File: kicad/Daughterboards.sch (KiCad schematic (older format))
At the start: 6 parts

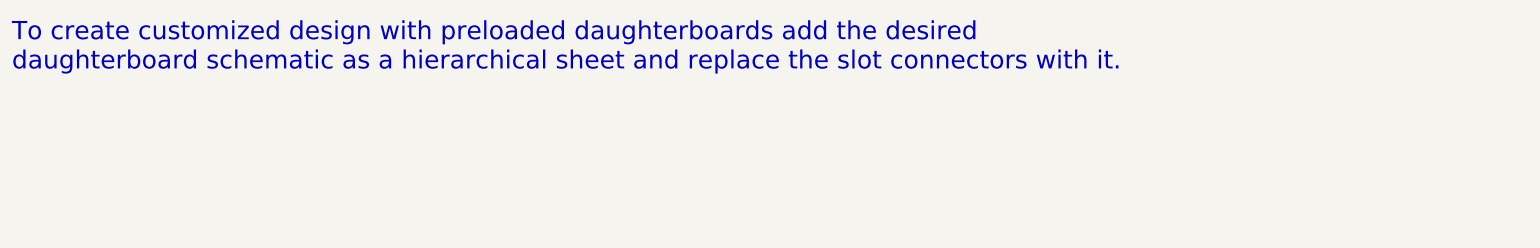
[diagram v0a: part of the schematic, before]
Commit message: Completed data and power isolation sheets
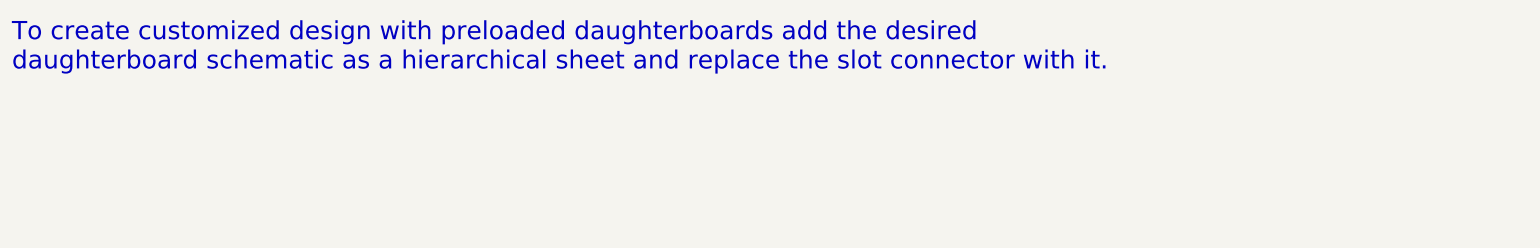
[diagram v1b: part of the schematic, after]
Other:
- note added: "To create customized design with preloaded daughterboards add the desired \ndaughterboard schematic as a hierarchical sheet and replace the slot connector with it."
- note removed: "To create customized design with preloaded daughterboards add the desired \ndaughterboard schematic as a hierarchical sheet and replace the slot connectors with it."
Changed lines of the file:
@@
 LIBS:+5v_iso
 LIBS:gnd_iso
+LIBS:roe-0505s
+LIBS:si8660
 LIBS:Main-cache
 EELAYER 27 0
@@
 	7400 5150 7550 5150
 Text Notes 1000 1150 0    120  ~ 0
-To create customized design with preloaded daughterboards add the desired \ndaughterboard schematic as a hierarchical sheet and replace the slot connectors with it.
+To create customized design with preloaded daughterboards add the desired \ndaughterboard schematic as a hierarchical sheet and replace the slot connector with it.
 Wire Wire Line
 	5700 4950 5850 4950

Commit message: ID detection changed from RC to EEPROM based, D.board pinout changed, PIC18F85J94 added
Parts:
- removed P?: SLOT0, symbol CONN_10
- removed P?: SLOT1, symbol CONN_10
- removed P?: SLOT2, symbol CONN_10
- removed P?: SLOT3, symbol CONN_10
- removed P?: SLOT4, symbol CONN_10
- removed P?: SLOT5, symbol CONN_10
- added P?: SLOT_A, symbol CONN_12
- added P?: SLOT_B, symbol CONN_12
- added P?: SLOT_C, symbol CONN_12
- added P?: SLOT_D, symbol CONN_12
- added P?: SLOT_E, symbol CONN_12
- added P?: SLOT_F, symbol CONN_12
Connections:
- net labels added: ID_3.3V, ID_GND, ID_SCL, ID_SDA, RTS3, VCC
- net labels removed: ID0, ID1, ID2, ID3, ID4, ID5, ID_COM, RT3, VCC_5V
- wire segments 60 -> 72
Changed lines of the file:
@@
 LIBS:si8660
 LIBS:pic16f1704
+LIBS:PIC18F85J94
+LIBS:24AA014
 LIBS:Main-cache
 EELAYER 27 0
@@
 $Descr A4 11693 8268
 encoding utf-8
-Sheet 7 8
+Sheet 7 7
 Title ""
-Date "22 jun 2014"
+Date "23 jun 2014"
 Rev ""
 Comp ""
@@
 Comment4 ""
 $EndDescr
-$Comp
-L CONN_10 P?
-U 1 1 53A642AA
-P 4500 3100
-F 0 "P?" V 4450 3100 60  0000 C CNN
-F 1 "SLOT0" V 4550 3100 60  0000 C CNN
-F 2 "" H 4500 3100 60  0000 C CNN
-F 3 "" H 4500 3100 60  0000 C CNN
-	1    4500 3100
-	1    0    0    -1
-$EndComp
 Text HLabel 4000 2750 0    60   Output ~ 0
 RX0
@@
 Wire Wire Line
 	4150 3150 4000 3150
+Text HLabel 4000 3250 0    60   Input ~ 0
+VCC
+Wire Wire Line
+	4000 3250 4150 3250
+Text HLabel 4000 3350 0    60   Input ~ 0
+GND
+Text HLabel 4000 3550 0    60   BiDi ~ 0
+ID_SDA
+Wire Wire Line
+	4000 3350 4150 3350
+Wire Wire Line
+	4000 3450 4150 3450
+Wire Wire Line
+	4000 3550 4150 3550
+Text Notes 1000 1150 0    120  ~ 0
+To create customized design with preloaded daughterboards add the desired \ndaughterboard schematic as a hierarchical sheet and replace the slot connector with it.
+Text HLabel 4000 3650 0    60   BiDi ~ 0
+ID_SCL
+Text Notes 3750 6650 0    60   ~ 0
+All pins at 5V TTL level
+$Comp
+L CONN_12 P?
+U 1 1 53B6335B
+P 4500 3200
+F 0 "P?" V 4450 3200 60  0000 C CNN
+F 1 "SLOT_A" V 4550 3200 60  0000 C CNN
+F 2 "" H 4500 3200 60  0000 C CNN
+F 3 "" H 4500 3200 60  0000 C CNN
+	1    4500 3200
+	1    0    0    -1
+$EndComp
+Wire Wire Line
+	4000 3650 4150 3650
 Text HLabel 4000 3450 0    60   Input ~ 0
-VCC_5V
-Wire Wire Line
-	4000 3250 4150 3250
-Text HLabel 4000 3550 0    60   Input ~ 0
-GND
-Text HLabel 4000 3250 0    60   BiDi ~ 0
-ID0
-Wire Wire Line
-	4000 3350 4150 3350
-Wire Wire Line
-	4000 3450 4150 3450
-Wire Wire Line
-	4000 3550 4150 3550
-$Comp
-L CONN_10 P?
-U 1 1 53A64390
-P 6200 3100
-F 0 "P?" V 6150 3100 60  0000 C CNN
-F 1 "SLOT1" V 6250 3100 60  0000 C CNN
-F 2 "" H 6200 3100 60  0000 C CNN
-F 3 "" H 6200 3100 60  0000 C CNN
-	1    6200 3100
-	1    0    0    -1
-$EndComp
+ID_3.3V
+Text HLabel 4000 3750 0    60   Input ~ 0
+ID_GND
+Wire Wire Line
+	4000 3750 4150 3750
 Text HLabel 5700 2750 0    60   Output ~ 0
 RX1
@@
 Wire Wire Line
 	5850 3150 5700 3150
+Text HLabel 5700 3250 0    60   Input ~ 0
+VCC
+Wire Wire Line
+	5700 3250 5850 3250
+Text HLabel 5700 3350 0    60   Input ~ 0
+GND
+Text HLabel 5700 3550 0    60   BiDi ~ 0
+ID_SDA
+Wire Wire Line
+	5700 3350 5850 3350
+Wire Wire Line
+	5700 3450 5850 3450
+Wire Wire Line
+	5700 3550 5850 3550
+Text HLabel 5700 3650 0    60   BiDi ~ 0
+ID_SCL
+$Comp
+L CONN_12 P?
+U 1 1 53B634CC
+P 6200 3200
+F 0 "P?" V 6150 3200 60  0000 C CNN
+F 1 "SLOT_B" V 6250 3200 60  0000 C CNN
+F 2 "" H 6200 3200 60  0000 C CNN
+F 3 "" H 6200 3200 60  0000 C CNN
+	1    6200 3200
+	1    0    0    -1
+$EndComp
+Wire Wire Line
+	5700 3650 5850 3650
 Text HLabel 5700 3450 0    60   Input ~ 0
-VCC_5V
-Wire Wire Line
-	5700 3250 5850 3250
-Text HLabel 5700 3550 0    60   Input ~ 0
-GND
-Text HLabel 5700 3250 0    60   BiDi ~ 0
-ID1
-Wire Wire Line
-	5700 3350 5850 3350
-Wire Wire Line
-	5700 3450 5850 3450
-Wire Wire Line
-	5700 3550 5850 3550
-$Comp
-L CONN_10 P?
-U 1 1 53A643DC
-P 7900 3100
-F 0 "P?" V 7850 3100 60  0000 C CNN
-F 1 "SLOT2" V 7950 3100 60  0000 C CNN
-F 2 "" H 7900 3100 60  0000 C CNN
-F 3 "" H 7900 3100 60  0000 C CNN
-	1    7900 3100
-	1    0    0    -1
-$EndComp
+ID_3.3V
+Text HLabel 5700 3750 0    60   Input ~ 0
+ID_GND
+Wire Wire Line
+	5700 3750 5850 3750
 Text HLabel 7400 2750 0    60   Output ~ 0
 RX2
@@
 Wire Wire Line
 	7550 3150 7400 3150
+Text HLabel 7400 3250 0    60   Input ~ 0
+VCC
+Wire Wire Line
+	7400 3250 7550 3250
+Text HLabel 7400 3350 0    60   Input ~ 0
+GND
+Text HLabel 7400 3550 0    60   BiDi ~ 0
+ID_SDA
+Wire Wire Line
+	7400 3350 7550 3350
+Wire Wire Line
+	7400 3450 7550 3450
+Wire Wire Line
+	7400 3550 7550 3550
+Text HLabel 7400 3650 0    60   BiDi ~ 0
+ID_SCL
+$Comp
+L CONN_12 P?
+U 1 1 53B634F5
+P 7900 3200
+F 0 "P?" V 7850 3200 60  0000 C CNN
+F 1 "SLOT_C" V 7950 3200 60  0000 C CNN
+F 2 "" H 7900 3200 60  0000 C CNN
+F 3 "" H 7900 3200 60  0000 C CNN
+	1    7900 3200
+	1    0    0    -1
+$EndComp
+Wire Wire Line
+	7400 3650 7550 3650
 Text HLabel 7400 3450 0    60   Input ~ 0
-VCC_5V
-Wire Wire Line
-	7400 3250 7550 3250
-Text HLabel 7400 3550 0    60   Input ~ 0
-GND
-Text HLabel 7400 3250 0    60   BiDi ~ 0
-ID2
-Wire Wire Line
-	7400 3350 7550 3350
-Wire Wire Line
-	7400 3450 7550 3450
-Wire Wire Line
-	7400 3550 7550 3550
-$Comp
-L CONN_10 P?
-U 1 1 53A643F6
-P 4500 4700
-F 0 "P?" V 4450 4700 60  0000 C CNN
-F 1 "SLOT3" V 4550 4700 60  0000 C CNN
-F 2 "" H 4500 4700 60  0000 C CNN
-F 3 "" H 4500 4700 60  0000 C CNN
-	1    4500 4700
-	1    0    0    -1
-$EndComp
+ID_3.3V
+Text HLabel 7400 3750 0    60   Input ~ 0
+ID_GND
+Wire Wire Line
+	7400 3750 7550 3750
 Text HLabel 4000 4350 0    60   Output ~ 0
 RX3
@@
 TX3
 Text HLabel 4000 4450 0    60   Input ~ 0
-RT3
+RTS3
 Text HLabel 4000 4550 0    60   Output ~ 0
 CTS3
@@
 Wire Wire Line
 	4150 4750 4000 4750
+Text HLabel 4000 4850 0    60   Input ~ 0
+VCC
+Wire Wire Line
+	4000 4850 4150 4850
+Text HLabel 4000 4950 0    60   Input ~ 0
+GND
+Text HLabel 4000 5150 0    60   BiDi ~ 0
+ID_SDA
+Wire Wire Line
+	4000 4950 4150 4950
+Wire Wire Line
+	4000 5050 4150 5050
+Wire Wire Line
+	4000 5150 4150 5150
+Text HLabel 4000 5250 0    60   BiDi ~ 0
+ID_SCL
+$Comp
+L CONN_12 P?
+U 1 1 53B63519
+P 4500 4800
+F 0 "P?" V 4450 4800 60  0000 C CNN
+F 1 "SLOT_D" V 4550 4800 60  0000 C CNN
+F 2 "" H 4500 4800 60  0000 C CNN
+F 3 "" H 4500 4800 60  0000 C CNN
+	1    4500 4800
+	1    0    0    -1
+$EndComp
+Wire Wire Line
+	4000 5250 4150 5250
 Text HLabel 4000 5050 0    60   Input ~ 0
-VCC_5V
-Wire Wire Line
-	4000 4850 4150 4850
-Text HLabel 4000 5150 0    60   Input ~ 0
-GND
-Text HLabel 4000 4850 0    60   BiDi ~ 0
-ID3
-Wire Wire Line
-	4000 4950 4150 4950
-Wire Wire Line
-	4000 5050 4150 5050
-Wire Wire Line
-	4000 5150 4150 5150
-$Comp
-L CONN_10 P?
-U 1 1 53A64410
-P 6200 4700
-F 0 "P?" V 6150 4700 60  0000 C CNN
-F 1 "SLOT4" V 6250 4700 60  0000 C CNN
-F 2 "" H 6200 4700 60  0000 C CNN
-F 3 "" H 6200 4700 60  0000 C CNN
-	1    6200 4700
-	1    0    0    -1
-$EndComp
+ID_3.3V
+Text HLabel 4000 5350 0    60   Input ~ 0
+ID_GND
+Wire Wire Line
+	4000 5350 4150 5350
 Text HLabel 5700 4350 0    60   Output ~ 0
 RX4
@@
 Wire Wire Line
 	5850 4750 5700 4750
+Text HLabel 5700 4850 0    60   Input ~ 0
+VCC
+Wire Wire Line
+	5700 4850 5850 4850
+Text HLabel 5700 4950 0    60   Input ~ 0
+GND
+Text HLabel 5700 5150 0    60   BiDi ~ 0
+ID_SDA
+Wire Wire Line
+	5700 4950 5850 4950
+Wire Wire Line
+	5700 5050 5850 5050
+Wire Wire Line
+	5700 5150 5850 5150
+Text HLabel 5700 5250 0    60   BiDi ~ 0
+ID_SCL
+$Comp
+L CONN_12 P?
+U 1 1 53B6353D
+P 6200 4800
+F 0 "P?" V 6150 4800 60  0000 C CNN
+F 1 "SLOT_E" V 6250 4800 60  0000 C CNN
+F 2 "" H 6200 4800 60  0000 C CNN
+F 3 "" H 6200 4800 60  0000 C CNN
+	1    6200 4800
+	1    0    0    -1
+$EndComp
+Wire Wire Line
+	5700 5250 5850 5250
 Text HLabel 5700 5050 0    60   Input ~ 0
-VCC_5V
-Wire Wire Line
-	5700 4850 5850 4850
-Text HLabel 5700 5150 0    60   Input ~ 0
-GND
-Text HLabel 5700 4850 0    60   BiDi ~ 0
-ID4
-Wire Wire Line
-	5700 5050 5850 5050
-Wire Wire Line
-	5700 5150 5850 5150
-$Comp
-L CONN_10 P?
-U 1 1 53A6442A
-P 7900 4700
-F 0 "P?" V 7850 4700 60  0000 C CNN
-F 1 "SLOT5" V 7950 4700 60  0000 C CNN
-F 2 "" H 7900 4700 60  0000 C CNN
-F 3 "" H 7900 4700 60  0000 C CNN
-	1    7900 4700
-	1    0    0    -1
-$EndComp
+ID_3.3V
+Text HLabel 5700 5350 0    60   Input ~ 0
+ID_GND
+Wire Wire Line
+	5700 5350 5850 5350
 Text HLabel 7400 4350 0    60   Output ~ 0
 RX5
@@
 Wire Wire Line
 	7550 4750 7400 4750
+Text HLabel 7400 4850 0    60   Input ~ 0
+VCC
+Wire Wire Line
+	7400 4850 7550 4850
+Text HLabel 7400 4950 0    60   Input ~ 0
+GND
+Text HLabel 7400 5150 0    60   BiDi ~ 0
+ID_SDA
+Wire Wire Line
+	7400 4950 7550 4950
+Wire Wire Line
+	7400 5050 7550 5050
+Wire Wire Line
+	7400 5150 7550 5150
+Text HLabel 7400 5250 0    60   BiDi ~ 0
+ID_SCL
+$Comp
+L CONN_12 P?
+U 1 1 53B63567
+P 7900 4800
+F 0 "P?" V 7850 4800 60  0000 C CNN
+F 1 "SLOT_F" V 7950 4800 60  0000 C CNN
+F 2 "" H 7900 4800 60  0000 C CNN
+F 3 "" H 7900 4800 60  0000 C CNN
+	1    7900 4800
+	1    0    0    -1
+$EndComp
+Wire Wire Line
+	7400 5250 7550 5250
 Text HLabel 7400 5050 0    60   Input ~ 0
-VCC_5V
-Wire Wire Line
-	7400 4850 7550 4850
-Text HLabel 7400 5150 0    60   Input ~ 0
-GND
-Text HLabel 7400 4850 0    60   BiDi ~ 0
-ID5
-Wire Wire Line
-	7400 4950 7550 4950
-Wire Wire Line
-	7400 5050 7550 5050
-Wire Wire Line
-	7400 5150 7550 5150
-Text Notes 1000 1150 0    120  ~ 0
-To create customized design with preloaded daughterboards add the desired \ndaughterboard schematic as a hierarchical sheet and replace the slot connector with it.
-Wire Wire Line
-	5700 4950 5850 4950
-Text HLabel 4000 3350 0    60   Input ~ 0
-ID_COM
-Text HLabel 5700 3350 0    60   Input ~ 0
-ID_COM
-Text HLabel 7400 3350 0    60   Input ~ 0
-ID_COM
-Text HLabel 4000 4950 0    60   Input ~ 0
-ID_COM
-Text HLabel 5700 4950 0    60   Input ~ 0
-ID_COM
-Text HLabel 7400 4950 0    60   Input ~ 0
-ID_COM
-Text Notes 3750 6650 0    60   ~ 0
-All pins at 5V TTL level
+ID_3.3V
+Text HLabel 7400 5350 0    60   Input ~ 0
+ID_GND
+Wire Wire Line
+	7400 5350 7550 5350
 $EndSCHEMATC

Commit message: Added NC pin to D.board pinout for better elec. isolation
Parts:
- removed P?: SLOT_A, symbol CONN_12
- removed P?: SLOT_B, symbol CONN_12
- removed P?: SLOT_C, symbol CONN_12
- removed P?: SLOT_D, symbol CONN_12
- removed P?: SLOT_E, symbol CONN_12
- removed P?: SLOT_F, symbol CONN_12
- added P?: SLOT_A, symbol CONN_13
- added P?: SLOT_B, symbol CONN_13
- added P?: SLOT_C, symbol CONN_13
- added P?: SLOT_D, symbol CONN_13
- added P?: SLOT_E, symbol CONN_13
- added P?: SLOT_F, symbol CONN_13
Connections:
- no-connect marks 0 -> 6
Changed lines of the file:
@@
 Text HLabel 4000 3350 0    60   Input ~ 0
 GND
-Text HLabel 4000 3550 0    60   BiDi ~ 0
+Text HLabel 4000 3650 0    60   BiDi ~ 0
 ID_SDA
 Wire Wire Line
 	4000 3350 4150 3350
 Wire Wire Line
-	4000 3450 4150 3450
-Wire Wire Line
 	4000 3550 4150 3550
+Wire Wire Line
+	4000 3650 4150 3650
 Text Notes 1000 1150 0    120  ~ 0
 To create customized design with preloaded daughterboards add the desired \ndaughterboard schematic as a hierarchical sheet and replace the slot connector with it.
-Text HLabel 4000 3650 0    60   BiDi ~ 0
+Text HLabel 4000 3750 0    60   BiDi ~ 0
 ID_SCL
 Text Notes 3750 6650 0    60   ~ 0
 All pins at 5V TTL level
-$Comp
-L CONN_12 P?
-U 1 1 53B6335B
-P 4500 3200
-F 0 "P?" V 4450 3200 60  0000 C CNN
-F 1 "SLOT_A" V 4550 3200 60  0000 C CNN
-F 2 "" H 4500 3200 60  0000 C CNN
-F 3 "" H 4500 3200 60  0000 C CNN
-	1    4500 3200
-	1    0    0    -1
-$EndComp
-Wire Wire Line
-	4000 3650 4150 3650
-Text HLabel 4000 3450 0    60   Input ~ 0
-ID_3.3V
-Text HLabel 4000 3750 0    60   Input ~ 0
-ID_GND
 Wire Wire Line
 	4000 3750 4150 3750
+Text HLabel 4000 3550 0    60   Input ~ 0
+ID_3.3V
+Text HLabel 4000 3850 0    60   Input ~ 0
+ID_GND
+Wire Wire Line
+	4000 3850 4150 3850
 Text HLabel 5700 2750 0    60   Output ~ 0
 RX1
@@
 Text HLabel 5700 3350 0    60   Input ~ 0
 GND
-Text HLabel 5700 3550 0    60   BiDi ~ 0
+Text HLabel 5700 3650 0    60   BiDi ~ 0
 ID_SDA
 Wire Wire Line
 	5700 3350 5850 3350
 Wire Wire Line
-	5700 3450 5850 3450
-Wire Wire Line
 	5700 3550 5850 3550
-Text HLabel 5700 3650 0    60   BiDi ~ 0
-ID_SCL
-$Comp
-L CONN_12 P?
-U 1 1 53B634CC
-P 6200 3200
-F 0 "P?" V 6150 3200 60  0000 C CNN
-F 1 "SLOT_B" V 6250 3200 60  0000 C CNN
-F 2 "" H 6200 3200 60  0000 C CNN
-F 3 "" H 6200 3200 60  0000 C CNN
-	1    6200 3200
-	1    0    0    -1
-$EndComp
 Wire Wire Line
 	5700 3650 5850 3650
-Text HLabel 5700 3450 0    60   Input ~ 0
-ID_3.3V
-Text HLabel 5700 3750 0    60   Input ~ 0
-ID_GND
+Text HLabel 5700 3750 0    60   BiDi ~ 0
+ID_SCL
 Wire Wire Line
 	5700 3750 5850 3750
+Text HLabel 5700 3550 0    60   Input ~ 0
+ID_3.3V
+Text HLabel 5700 3850 0    60   Input ~ 0
+ID_GND
+Wire Wire Line
+	5700 3850 5850 3850
 Text HLabel 7400 2750 0    60   Output ~ 0
 RX2
@@
 Text HLabel 7400 3350 0    60   Input ~ 0
 GND
-Text HLabel 7400 3550 0    60   BiDi ~ 0
+Text HLabel 7400 3650 0    60   BiDi ~ 0
 ID_SDA
 Wire Wire Line
 	7400 3350 7550 3350
 Wire Wire Line
-	7400 3450 7550 3450
-Wire Wire Line
 	7400 3550 7550 3550
-Text HLabel 7400 3650 0    60   BiDi ~ 0
-ID_SCL
-$Comp
-L CONN_12 P?
-U 1 1 53B634F5
-P 7900 3200
-F 0 "P?" V 7850 3200 60  0000 C CNN
-F 1 "SLOT_C" V 7950 3200 60  0000 C CNN
-F 2 "" H 7900 3200 60  0000 C CNN
-F 3 "" H 7900 3200 60  0000 C CNN
-	1    7900 3200
-	1    0    0    -1
-$EndComp
 Wire Wire Line
 	7400 3650 7550 3650
-Text HLabel 7400 3450 0    60   Input ~ 0
-ID_3.3V
-Text HLabel 7400 3750 0    60   Input ~ 0
-ID_GND
+Text HLabel 7400 3750 0    60   BiDi ~ 0
+ID_SCL
 Wire Wire Line
 	7400 3750 7550 3750
+Text HLabel 7400 3550 0    60   Input ~ 0
+ID_3.3V
+Text HLabel 7400 3850 0    60   Input ~ 0
+ID_GND
+Wire Wire Line
+	7400 3850 7550 3850
 Text HLabel 4000 4350 0    60   Output ~ 0
 RX3
@@
 Text HLabel 4000 4950 0    60   Input ~ 0
 GND
-Text HLabel 4000 5150 0    60   BiDi ~ 0
+Text HLabel 4000 5250 0    60   BiDi ~ 0
 ID_SDA
 Wire Wire Line
 	4000 4950 4150 4950
 Wire Wire Line
-	4000 5050 4150 5050
-Wire Wire Line
 	4000 5150 4150 5150
-Text HLabel 4000 5250 0    60   BiDi ~ 0
-ID_SCL
-$Comp
-L CONN_12 P?
-U 1 1 53B63519
-P 4500 4800
-F 0 "P?" V 4450 4800 60  0000 C CNN
-F 1 "SLOT_D" V 4550 4800 60  0000 C CNN
-F 2 "" H 4500 4800 60  0000 C CNN
-F 3 "" H 4500 4800 60  0000 C CNN
-	1    4500 4800
-	1    0    0    -1
-$EndComp
 Wire Wire Line
 	4000 5250 4150 5250
-Text HLabel 4000 5050 0    60   Input ~ 0
-ID_3.3V
-Text HLabel 4000 5350 0    60   Input ~ 0
-ID_GND
+Text HLabel 4000 5350 0    60   BiDi ~ 0
+ID_SCL
 Wire Wire Line
 	4000 5350 4150 5350
+Text HLabel 4000 5150 0    60   Input ~ 0
+ID_3.3V
+Text HLabel 4000 5450 0    60   Input ~ 0
+ID_GND
+Wire Wire Line
+	4000 5450 4150 5450
 Text HLabel 5700 4350 0    60   Output ~ 0
 RX4
@@
 Text HLabel 5700 4950 0    60   Input ~ 0
 GND
-Text HLabel 5700 5150 0    60   BiDi ~ 0
+Text HLabel 5700 5250 0    60   BiDi ~ 0
 ID_SDA
 Wire Wire Line
 	5700 4950 5850 4950
 Wire Wire Line
-	5700 5050 5850 5050
-Wire Wire Line
 	5700 5150 5850 5150
-Text HLabel 5700 5250 0    60   BiDi ~ 0
-ID_SCL
-$Comp
-L CONN_12 P?
-U 1 1 53B6353D
-P 6200 4800
-F 0 "P?" V 6150 4800 60  0000 C CNN
-F 1 "SLOT_E" V 6250 4800 60  0000 C CNN
-F 2 "" H 6200 4800 60  0000 C CNN
-F 3 "" H 6200 4800 60  0000 C CNN
-	1    6200 4800
-	1    0    0    -1
-$EndComp
 Wire Wire Line
 	5700 5250 5850 5250
-Text HLabel 5700 5050 0    60   Input ~ 0
-ID_3.3V
-Text HLabel 5700 5350 0    60   Input ~ 0
-ID_GND
+Text HLabel 5700 5350 0    60   BiDi ~ 0
+ID_SCL
 Wire Wire Line
 	5700 5350 5850 5350
+Text HLabel 5700 5150 0    60   Input ~ 0
+ID_3.3V
+Text HLabel 5700 5450 0    60   Input ~ 0
+ID_GND
+Wire Wire Line
+	5700 5450 5850 5450
 Text HLabel 7400 4350 0    60   Output ~ 0
 RX5
@@
 Text HLabel 7400 4950 0    60   Input ~ 0
 GND
-Text HLabel 7400 5150 0    60   BiDi ~ 0
+Text HLabel 7400 5250 0    60   BiDi ~ 0
 ID_SDA
 Wire Wire Line
 	7400 4950 7550 4950
 Wire Wire Line
-	7400 5050 7550 5050
-Wire Wire Line
 	7400 5150 7550 5150
-Text HLabel 7400 5250 0    60   BiDi ~ 0
-ID_SCL
-$Comp
-L CONN_12 P?
-U 1 1 53B63567
-P 7900 4800
-F 0 "P?" V 7850 4800 60  0000 C CNN
-F 1 "SLOT_F" V 7950 4800 60  0000 C CNN
-F 2 "" H 7900 4800 60  0000 C CNN
-F 3 "" H 7900 4800 60  0000 C CNN
-	1    7900 4800
-	1    0    0    -1
-$EndComp
 Wire Wire Line
 	7400 5250 7550 5250
-Text HLabel 7400 5050 0    60   Input ~ 0
-ID_3.3V
-Text HLabel 7400 5350 0    60   Input ~ 0
-ID_GND
+Text HLabel 7400 5350 0    60   BiDi ~ 0
+ID_SCL
 Wire Wire Line
 	7400 5350 7550 5350
+Text HLabel 7400 5150 0    60   Input ~ 0
+ID_3.3V
+Text HLabel 7400 5450 0    60   Input ~ 0
+ID_GND
+Wire Wire Line
+	7400 5450 7550 5450
+$Comp
+L CONN_13 P?
+U 1 1 53B751DE
+P 4500 3250
+F 0 "P?" V 4460 3250 60  0000 C CNN
+F 1 "SLOT_A" V 4570 3250 60  0000 C CNN
+F 2 "" H 4500 3250 60  0000 C CNN
+F 3 "" H 4500 3250 60  0000 C CNN
+	1    4500 3250
+	1    0    0    -1
+$EndComp
+$Comp
+L CONN_13 P?
+U 1 1 53B751F7
+P 6200 3250
+F 0 "P?" V 6160 3250 60  0000 C CNN
+F 1 "SLOT_B" V 6270 3250 60  0000 C CNN
+F 2 "" H 6200 3250 60  0000 C CNN
+F 3 "" H 6200 3250 60  0000 C CNN
+	1    6200 3250
+	1    0    0    -1
+$EndComp
+$Comp
+L CONN_13 P?
+U 1 1 53B75207
+P 7900 3250
+F 0 "P?" V 7860 3250 60  0000 C CNN
+F 1 "SLOT_C" V 7970 3250 60  0000 C CNN
+F 2 "" H 7900 3250 60  0000 C CNN
+F 3 "" H 7900 3250 60  0000 C CNN
+	1    7900 3250
+	1    0    0    -1
+$EndComp
+$Comp
+L CONN_13 P?
+U 1 1 53B7520D
+P 4500 4850
+F 0 "P?" V 4460 4850 60  0000 C CNN
+F 1 "SLOT_D" V 4570 4850 60  0000 C CNN
+F 2 "" H 4500 4850 60  0000 C CNN
+F 3 "" H 4500 4850 60  0000 C CNN
+	1    4500 4850
+	1    0    0    -1
+$EndComp
+$Comp
+L CONN_13 P?
+U 1 1 53B75213
+P 6200 4850
+F 0 "P?" V 6160 4850 60  0000 C CNN
+F 1 "SLOT_E" V 6270 4850 60  0000 C CNN
+F 2 "" H 6200 4850 60  0000 C CNN
+F 3 "" H 6200 4850 60  0000 C CNN
+	1    6200 4850
+	1    0    0    -1
+$EndComp
+$Comp
+L CONN_13 P?
+U 1 1 53B75219
+P 7900 4850
+F 0 "P?" V 7860 4850 60  0000 C CNN
+F 1 "SLOT_F" V 7970 4850 60  0000 C CNN
+F 2 "" H 7900 4850 60  0000 C CNN
+F 3 "" H 7900 4850 60  0000 C CNN
+	1    7900 4850
+	1    0    0    -1
+$EndComp
+NoConn ~ 4150 3450
+NoConn ~ 5850 3450
+NoConn ~ 7550 3450
+NoConn ~ 4150 5050
+NoConn ~ 5850 5050
+NoConn ~ 7550 5050
 $EndSCHEMATC
